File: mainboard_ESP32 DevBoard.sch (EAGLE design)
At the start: 44 parts, among them IC1 OP-AMP-2-LONG, K1 AQH213, T1 2N2222, X1 JST-XH-02-PIN-LONG-PAD, X2 JST-XH-04-PIN-LONG-PAD, X3 1751293, X4 JST-XH-04-PIN-LONG-PAD

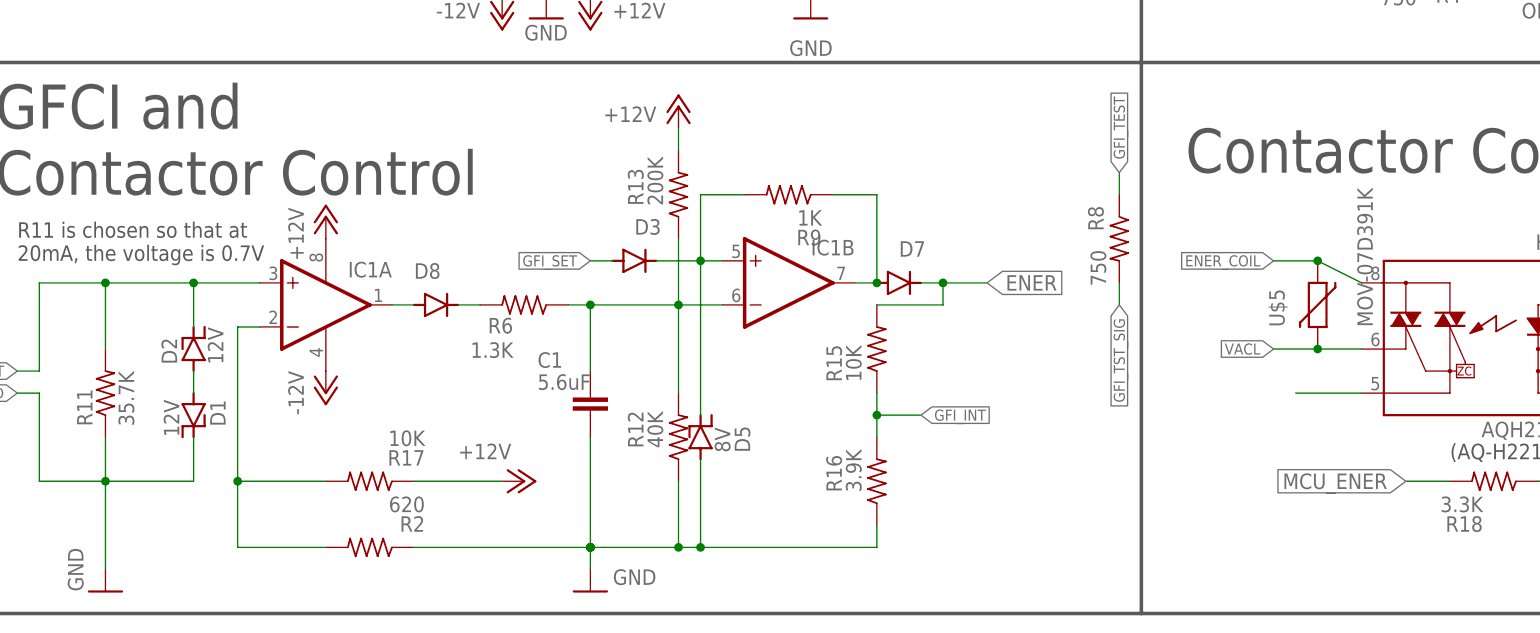
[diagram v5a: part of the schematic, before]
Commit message: Completed new GFCI circuit
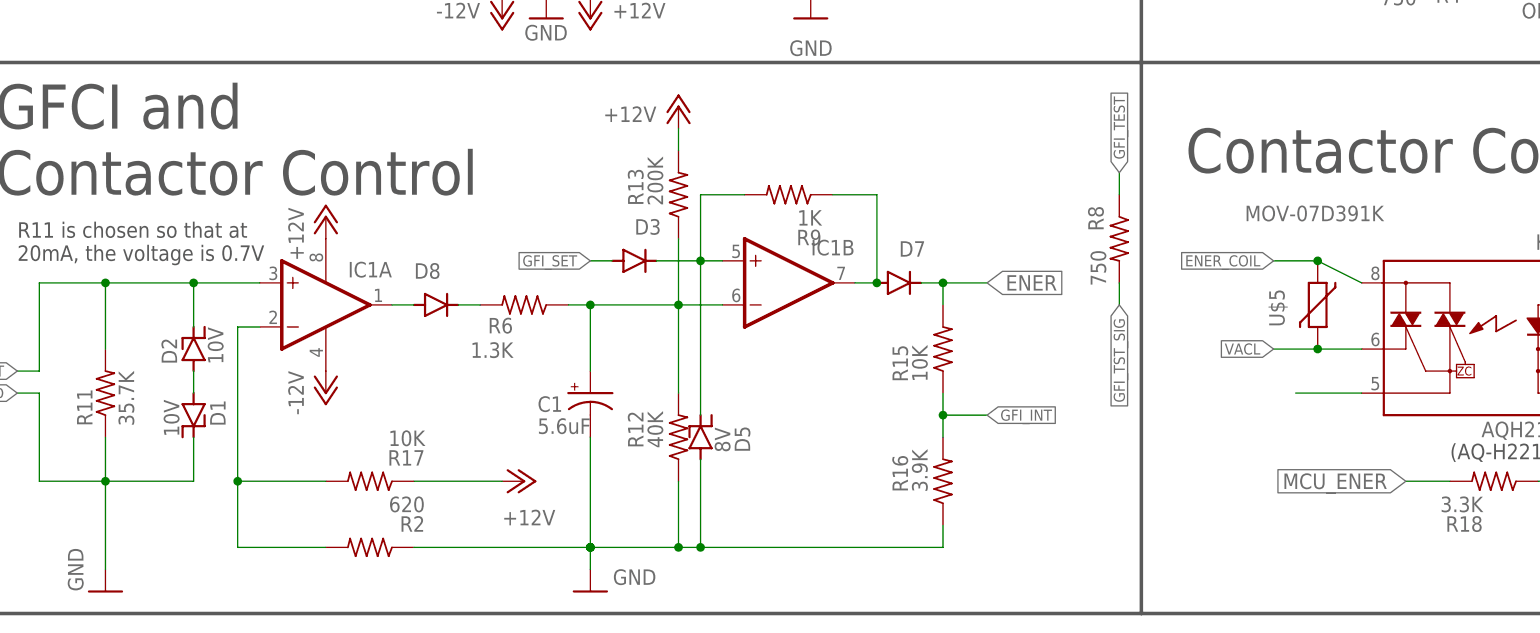
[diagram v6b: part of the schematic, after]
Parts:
- C1: device rcl:C-EU025-025X050 -> rcl:CPOL-USE2-5
- D1, D2: value 12V -> 10V
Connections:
- net GND: now also C1.-; no longer C1.2
- net N$9: now also C1.+; no longer C1.1
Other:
- moved on the sheet: R15, R16
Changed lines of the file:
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@@
 <part name="R10" library="Passive" deviceset="RESISTOR" device="L" value="24K"/>
 <part name="+3V6" library="supply1" library_urn="urn:adsk.eagle:library:371" deviceset="+3V3" device=""/>
-<part name="D1" library="Passive" deviceset="ZENER" device="" value="12V"/>
-<part name="D2" library="Passive" deviceset="ZENER" device="" value="12V"/>
+<part name="D1" library="Passive" deviceset="ZENER" device="" value="10V"/>
+<part name="D2" library="Passive" deviceset="ZENER" device="" value="10V"/>
 <part name="IC1" library="Op Amp" deviceset="OP-AMP-2" device="-LONG"/>
 <part name="R11" library="Passive" deviceset="RESISTOR" device="L" value="35.7K"/>
@@
 <part name="D8" library="diode" library_urn="urn:adsk.eagle:library:210" deviceset="1N4148" device="DO35-7" package3d_urn="urn:adsk.eagle:package:43339/2"/>
 <part name="R6" library="Passive" deviceset="RESISTOR" device="L" value="1.3K"/>
-<part name="C1" library="rcl" library_urn="urn:adsk.eagle:library:334" deviceset="C-EU" device="025-025X050" package3d_urn="urn:adsk.eagle:package:23629/2" value="5.6uF"/>
+<part name="C1" library="rcl" library_urn="urn:adsk.eagle:library:334" deviceset="CPOL-US" device="E2-5" package3d_urn="urn:adsk.eagle:package:23346/2" value="5.6uF"/>
 <part name="R9" library="Passive" deviceset="RESISTOR" device="L" value="1K"/>
 <part name="D5" library="Passive" deviceset="ZENER" device="" value="8V"/>
@@
 <attribute name="VALUE" x="74.422" y="-44.45" size="1.778" layer="96" rot="R90"/>
 </instance>
-<instance part="R15" gate="G$1" x="99.06" y="-60.96" smashed="yes" rot="R90">
-<attribute name="NAME" x="95.0214" y="-64.77" size="1.778" layer="95" rot="R90"/>
-<attribute name="VALUE" x="97.282" y="-64.77" size="1.778" layer="96" rot="R90"/>
-</instance>
-<instance part="R16" gate="G$1" x="99.06" y="-76.2" smashed="yes" rot="R90">
-<attribute name="NAME" x="95.0214" y="-77.47" size="1.778" layer="95" rot="R90"/>
-<attribute name="VALUE" x="97.282" y="-77.47" size="1.778" layer="96" rot="R90"/>
+<instance part="R15" gate="G$1" x="106.68" y="-60.96" smashed="yes" rot="R90">
+<attribute name="NAME" x="102.6414" y="-64.77" size="1.778" layer="95" rot="R90"/>
+<attribute name="VALUE" x="104.902" y="-64.77" size="1.778" layer="96" rot="R90"/>
+</instance>
+<instance part="R16" gate="G$1" x="106.68" y="-76.2" smashed="yes" rot="R90">
+<attribute name="NAME" x="102.6414" y="-77.47" size="1.778" layer="95" rot="R90"/>
+<attribute name="VALUE" x="104.902" y="-77.47" size="1.778" layer="96" rot="R90"/>
 </instance>
 <instance part="R17" gate="G$1" x="40.64" y="-76.2" smashed="yes" rot="R180">
@@
 </instance>
 <instance part="P+7" gate="1" x="58.42" y="-76.2" smashed="yes" rot="R270">
-<attribute name="VALUE" x="50.8" y="-73.66" size="1.778" layer="96"/>
+<attribute name="VALUE" x="55.88" y="-81.28" size="1.778" layer="96"/>
 </instance>
 <instance part="D7" gate="G$1" x="101.6" y="-53.34" smashed="yes">
@@
 <instance part="U$5" gate="G$1" x="149.86" y="-55.88" smashed="yes" rot="R90">
 <attribute name="NAME" x="146.05" y="-58.42" size="1.778" layer="95" rot="R90"/>
-<attribute name="VALUE" x="156.21" y="-58.42" size="1.778" layer="96" rot="R90"/>
+<attribute name="VALUE" x="157.48" y="-44.45" size="1.778" layer="96" rot="R180"/>
 </instance>
 <instance part="D8" gate="G$1" x="48.26" y="-55.88" smashed="yes">
@@
 </instance>
 <instance part="C1" gate="G$1" x="66.04" y="-66.04" smashed="yes">
-<attribute name="NAME" x="59.944" y="-63.119" size="1.778" layer="95"/>
-<attribute name="VALUE" x="59.944" y="-65.659" size="1.778" layer="96"/>
+<attribute name="NAME" x="59.944" y="-68.199" size="1.778" layer="95"/>
+<attribute name="VALUE" x="59.944" y="-70.739" size="1.778" layer="96"/>
 </instance>
 <instance part="R9" gate="G$1" x="88.9" y="-43.18" smashed="yes" rot="R180">
@@
 <junction x="66.04" y="-83.82"/>
 <pinref part="R16" gate="G$1" pin="1"/>
-<wire x1="99.06" y1="-81.28" x2="99.06" y2="-83.82" width="0.1524" layer="91"/>
-<wire x1="99.06" y1="-83.82" x2="78.74" y2="-83.82" width="0.1524" layer="91"/>
+<wire x1="106.68" y1="-81.28" x2="106.68" y2="-83.82" width="0.1524" layer="91"/>
+<wire x1="106.68" y1="-83.82" x2="78.74" y2="-83.82" width="0.1524" layer="91"/>
 <junction x="66.04" y="-83.82"/>
 <pinref part="R12" gate="G$1" pin="1"/>
@@
 <wire x1="45.72" y1="-83.82" x2="66.04" y2="-83.82" width="0.1524" layer="91"/>
 <pinref part="R2" gate="G$1" pin="1"/>
-<pinref part="C1" gate="G$1" pin="2"/>
+<pinref part="C1" gate="G$1" pin="-"/>
 <wire x1="66.04" y1="-71.12" x2="66.04" y2="-83.82" width="0.1524" layer="91"/>
 <junction x="66.04" y="-83.82"/>
@@
 <wire x1="63.5" y1="-55.88" x2="66.04" y2="-55.88" width="0.1524" layer="91"/>
 <pinref part="R6" gate="G$1" pin="1"/>
-<pinref part="C1" gate="G$1" pin="1"/>
+<pinref part="C1" gate="G$1" pin="+"/>
 <wire x1="66.04" y1="-63.5" x2="66.04" y2="-55.88" width="0.1524" layer="91"/>
 <junction x="66.04" y="-55.88"/>
@@
 <pinref part="R15" gate="G$1" pin="1"/>
 <pinref part="R16" gate="G$1" pin="2"/>
-<wire x1="99.06" y1="-66.04" x2="99.06" y2="-68.58" width="0.1524" layer="91"/>
-<wire x1="99.06" y1="-68.58" x2="99.06" y2="-71.12" width="0.1524" layer="91"/>
-<wire x1="99.06" y1="-68.58" x2="104.14" y2="-68.58" width="0.1524" layer="91"/>
-<junction x="99.06" y="-68.58"/>
-<label x="104.14" y="-68.58" size="1.27" layer="95" xref="yes"/>
+<wire x1="106.68" y1="-66.04" x2="106.68" y2="-68.58" width="0.1524" layer="91"/>
+<wire x1="106.68" y1="-68.58" x2="106.68" y2="-71.12" width="0.1524" layer="91"/>
+<wire x1="106.68" y1="-68.58" x2="111.76" y2="-68.58" width="0.1524" layer="91"/>
+<junction x="106.68" y="-68.58"/>
+<label x="111.76" y="-68.58" size="1.27" layer="95" xref="yes"/>
 </segment>
 <segment>
@@
 <wire x1="106.68" y1="-53.34" x2="106.68" y2="-55.88" width="0.1524" layer="91"/>
 <pinref part="R15" gate="G$1" pin="2"/>
-<wire x1="106.68" y1="-55.88" x2="99.06" y2="-55.88" width="0.1524" layer="91"/>
 <wire x1="106.68" y1="-53.34" x2="111.76" y2="-53.34" width="0.1524" layer="91"/>
 <junction x="106.68" y="-53.34"/>

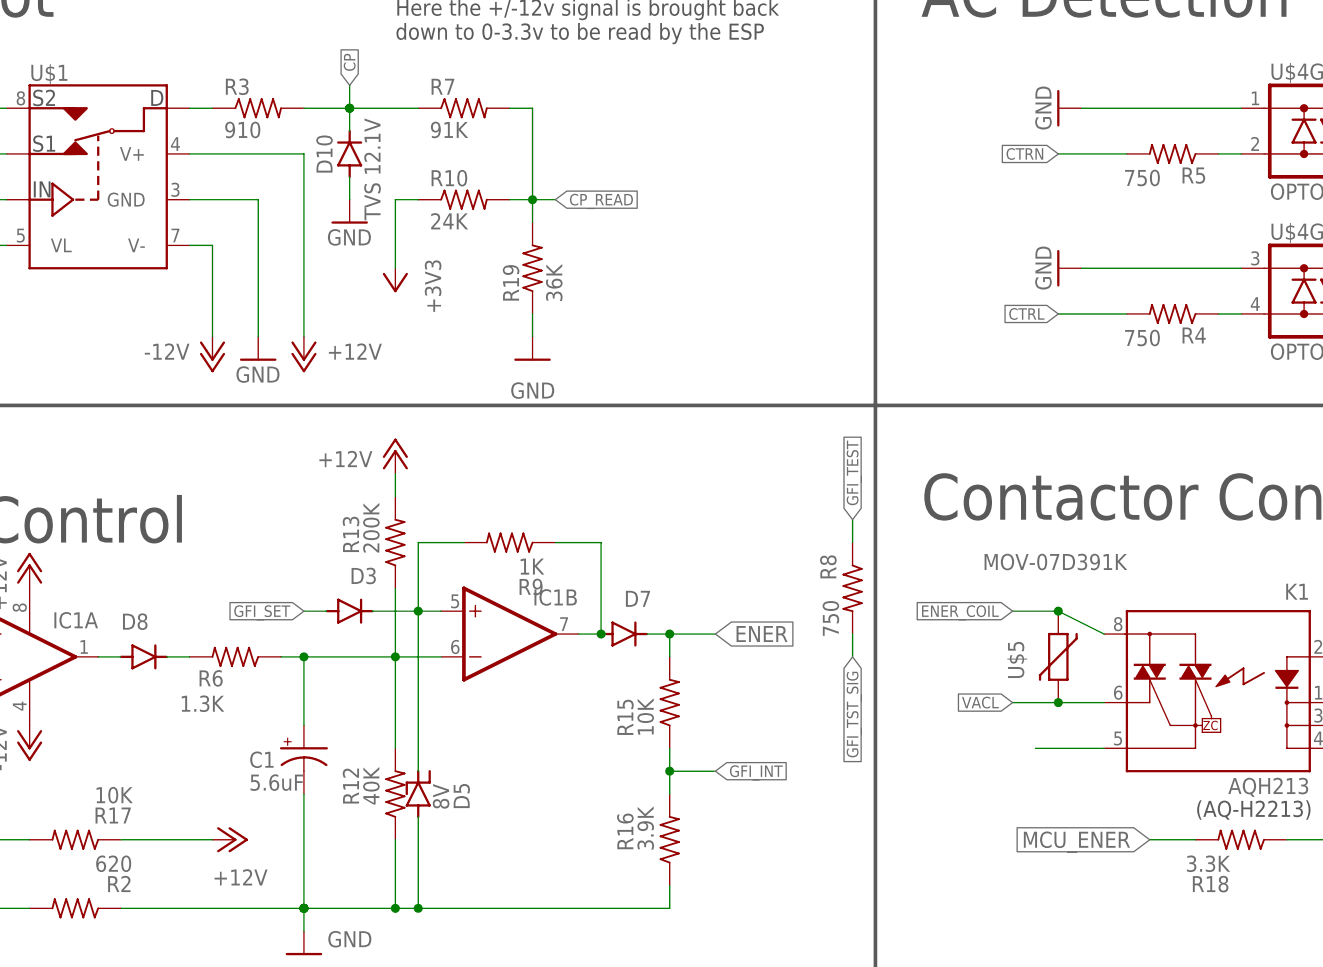
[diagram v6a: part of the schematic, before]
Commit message: Corrected some component values that were wrong during assembly
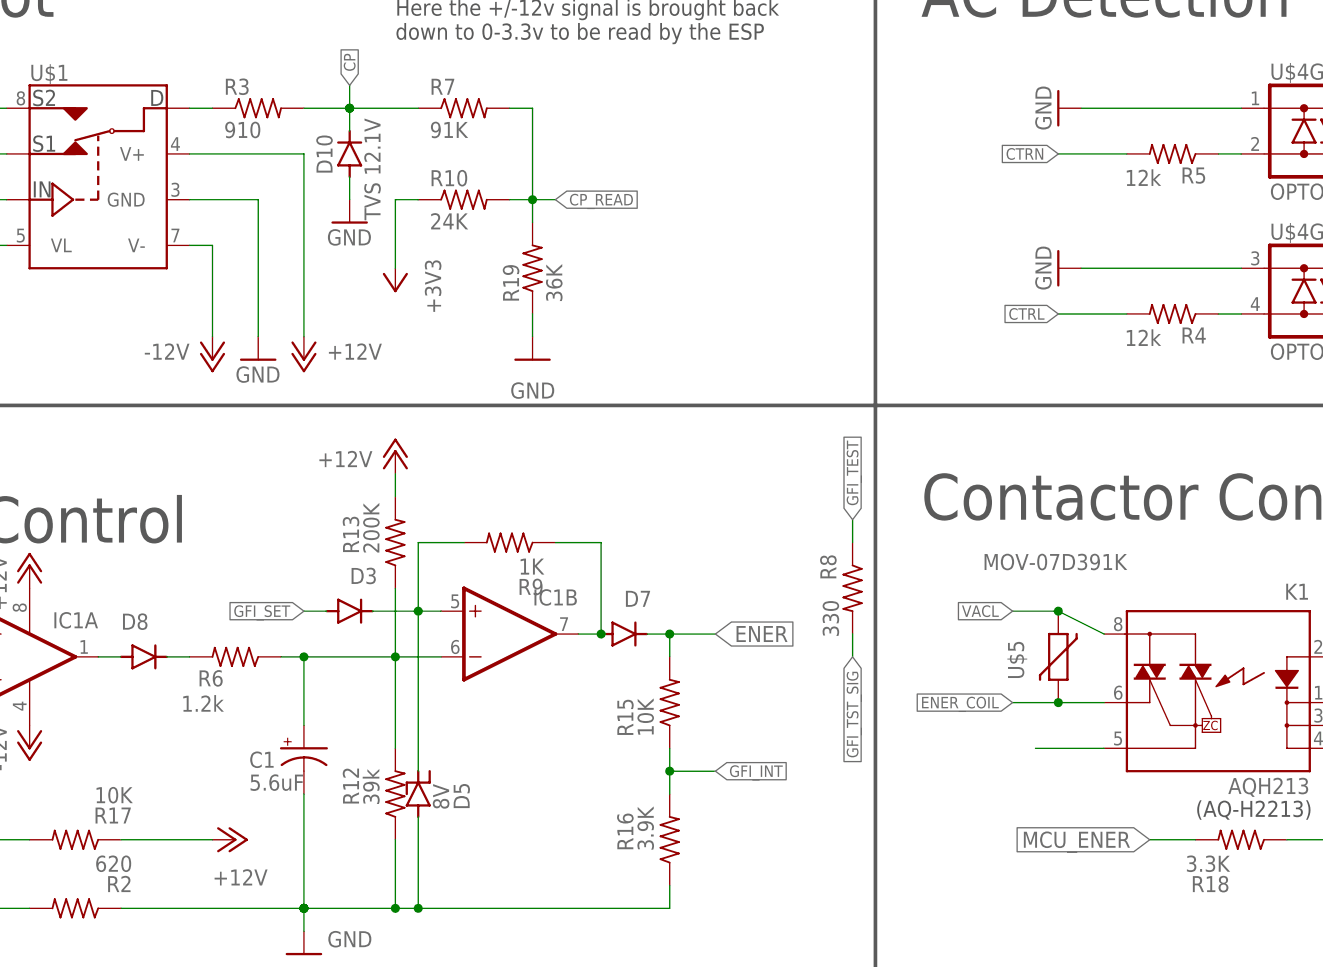
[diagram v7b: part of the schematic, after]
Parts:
- R12: value 40K -> 39k
- R4, R5: value 750 -> 12k
- R6: value 1.3K -> 1.2k
- R8: value 750 -> 330
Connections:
- net ENER_COIL: now also K1.DS3, U$5.2; no longer K1.DS1, U$5.1
- net VACL: now also K1.DS1, U$5.1; no longer K1.DS3, U$5.2
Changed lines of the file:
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@@
 <part name="R11" library="Passive" deviceset="RESISTOR" device="L" value="35.7K"/>
 <part name="D3" library="diode" library_urn="urn:adsk.eagle:library:210" deviceset="1N4148" device="DO35-7" package3d_urn="urn:adsk.eagle:package:43339/2"/>
-<part name="R12" library="Passive" deviceset="RESISTOR" device="L" value="40K"/>
+<part name="R12" library="Passive" deviceset="RESISTOR" device="L" value="39k"/>
 <part name="R13" library="Passive" deviceset="RESISTOR" device="L" value="200K"/>
 <part name="R15" library="Passive" deviceset="RESISTOR" device="L" value="10K"/>
@@
 <part name="D7" library="diode" library_urn="urn:adsk.eagle:library:210" deviceset="1N4148" device="DO35-7" package3d_urn="urn:adsk.eagle:package:43339/2"/>
 <part name="JP2" library="pinhead" library_urn="urn:adsk.eagle:library:325" deviceset="PINHD-1X2" device="/90" package3d_urn="urn:adsk.eagle:package:22437/2"/>
-<part name="R8" library="Passive" deviceset="RESISTOR" device="L" value="750"/>
+<part name="R8" library="Passive" deviceset="RESISTOR" device="L" value="330"/>
 <part name="X4" library="Rembrandt Electronics - JST XH Connectors v1-0" deviceset="JST-XH-04-PIN" device="-LONG-PAD"/>
 <part name="GND7" library="supply1" library_urn="urn:adsk.eagle:library:371" deviceset="GND" device=""/>
@@
 <part name="GND13" library="supply1" library_urn="urn:adsk.eagle:library:371" deviceset="GND" device=""/>
 <part name="U$4" library="optocouplers" deviceset="OPTOCOUPLER-2" device=""/>
-<part name="R4" library="Passive" deviceset="RESISTOR" device="L" value="750"/>
-<part name="R5" library="Passive" deviceset="RESISTOR" device="L" value="750"/>
+<part name="R4" library="Passive" deviceset="RESISTOR" device="L" value="12k"/>
+<part name="R5" library="Passive" deviceset="RESISTOR" device="L" value="12k"/>
 <part name="GND16" library="supply1" library_urn="urn:adsk.eagle:library:371" deviceset="GND" device=""/>
 <part name="GND17" library="supply1" library_urn="urn:adsk.eagle:library:371" deviceset="GND" device=""/>
@@
 <part name="U$5" library="EVSE" deviceset="MOV-07D391K" device=""/>
 <part name="D8" library="diode" library_urn="urn:adsk.eagle:library:210" deviceset="1N4148" device="DO35-7" package3d_urn="urn:adsk.eagle:package:43339/2"/>
-<part name="R6" library="Passive" deviceset="RESISTOR" device="L" value="1.3K"/>
+<part name="R6" library="Passive" deviceset="RESISTOR" device="L" value="1.2k"/>
 <part name="C1" library="rcl" library_urn="urn:adsk.eagle:library:334" deviceset="CPOL-US" device="E2-5" package3d_urn="urn:adsk.eagle:package:23346/2" value="5.6uF"/>
 <part name="R9" library="Passive" deviceset="RESISTOR" device="L" value="1K"/>
@@
 <net name="ENER_COIL" class="1">
 <segment>
-<pinref part="K1" gate="G$1" pin="DS1"/>
-<wire x1="154.94" y1="-53.34" x2="149.86" y2="-50.8" width="0.1524" layer="91"/>
-<label x="144.78" y="-50.8" size="1.27" layer="95" rot="R180" xref="yes"/>
-<pinref part="U$5" gate="G$1" pin="1"/>
-<wire x1="149.86" y1="-50.8" x2="144.78" y2="-50.8" width="0.1524" layer="91"/>
-<junction x="149.86" y="-50.8"/>
-</segment>
-<segment>
 <pinref part="X3" gate="-4" pin="K"/>
 <wire x1="175.26" y1="121.92" x2="175.26" y2="124.46" width="0.1524" layer="91"/>
 <label x="175.26" y="121.92" size="1.27" layer="95" rot="R270" xref="yes"/>
+</segment>
+<segment>
+<pinref part="K1" gate="G$1" pin="DS3"/>
+<wire x1="154.94" y1="-60.96" x2="149.86" y2="-60.96" width="0.1524" layer="91"/>
+<label x="144.78" y="-60.96" size="1.27" layer="95" rot="R180" xref="yes"/>
+<pinref part="U$5" gate="G$1" pin="2"/>
+<wire x1="149.86" y1="-60.96" x2="144.78" y2="-60.96" width="0.1524" layer="91"/>
+<junction x="149.86" y="-60.96"/>
 </segment>
 </net>
@@
 </segment>
 <segment>
-<pinref part="K1" gate="G$1" pin="DS3"/>
-<wire x1="154.94" y1="-60.96" x2="149.86" y2="-60.96" width="0.1524" layer="91"/>
-<label x="144.78" y="-60.96" size="1.27" layer="95" rot="R180" xref="yes"/>
-<pinref part="U$5" gate="G$1" pin="2"/>
-<wire x1="149.86" y1="-60.96" x2="144.78" y2="-60.96" width="0.1524" layer="91"/>
-<junction x="149.86" y="-60.96"/>
-</segment>
-<segment>
 <pinref part="X3" gate="-7" pin="K"/>
 <wire x1="182.88" y1="121.92" x2="182.88" y2="124.46" width="0.1524" layer="91"/>
 <label x="182.88" y="121.92" size="1.27" layer="95" rot="R270" xref="yes"/>
 </segment>
-</net>
+<segment>
+<pinref part="K1" gate="G$1" pin="DS1"/>
+<wire x1="154.94" y1="-53.34" x2="149.86" y2="-50.8" width="0.1524" layer="91"/>
+<label x="144.78" y="-50.8" size="1.27" layer="95" rot="R180" xref="yes"/>
+<pinref part="U$5" gate="G$1" pin="1"/>
+<wire x1="149.86" y1="-50.8" x2="144.78" y2="-50.8" width="0.1524" layer="91"/>
+<junction x="149.86" y="-50.8"/>
+</segment>
+</net>
